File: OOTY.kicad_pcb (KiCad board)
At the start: 2 copper layers, 0 parts

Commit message: phase 3: PCB setup (85x55 mm, 4 layers, rules, connectors placed), DRC 0 errors
Co-Authored-By: Claude Opus 5.5 <noreply@anthropic.com>
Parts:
- added C1: 100nF/50V, Capacitor_SMD:C_0402_1005Metric, F.Cu at (196.4, 101.0)
- added C10: 10uF/25V, Capacitor_SMD:C_0805_2012Metric, F.Cu at (227.4, 101.5)
- added C11: 100nF/50V, Capacitor_SMD:C_0402_1005Metric, F.Cu at (231.0, 101.0)
- added C12: 100nF/50V, Capacitor_SMD:C_0402_1005Metric, F.Cu at (233.9, 101.0)
- added C13: 10uF/25V, Capacitor_SMD:C_0805_2012Metric, F.Cu at (237.5, 101.5)
- added C14: 100nF/50V, Capacitor_SMD:C_0402_1005Metric, F.Cu at (241.2, 101.0)
- added C15: 100nF/50V, Capacitor_SMD:C_0402_1005Metric, F.Cu at (244.1, 101.0)
- added C16: 10uF/10V, Capacitor_SMD:C_0603_1608Metric, F.Cu at (247.5, 101.3)
- added C17: 100nF/50V, Capacitor_SMD:C_0402_1005Metric, F.Cu at (251.0, 101.0)
- added C18: 100nF/50V, Capacitor_SMD:C_0402_1005Metric, F.Cu at (253.8, 101.0)
- added C19: 10uF/10V, Capacitor_SMD:C_0603_1608Metric, F.Cu at (257.3, 101.3)
- added C2: 100nF/50V, Capacitor_SMD:C_0402_1005Metric, F.Cu at (199.3, 101.0)
- added C20: 100nF/50V, Capacitor_SMD:C_0402_1005Metric, F.Cu at (253.9, 104.0)
- added C21: 100nF/50V, Capacitor_SMD:C_0402_1005Metric, F.Cu at (256.8, 104.0)
- added C22: 100nF/50V, Capacitor_SMD:C_0402_1005Metric, F.Cu at (259.7, 104.0)
- added C23: 100nF/50V, Capacitor_SMD:C_0402_1005Metric, F.Cu at (262.5, 104.0)
- added C24: 4.7uF/16V, Capacitor_SMD:C_0603_1608Metric, F.Cu at (266.0, 104.3)
- added C25: 100nF/50V, Capacitor_SMD:C_0402_1005Metric, F.Cu at (269.4, 104.0)
- added C26: 10nF/50V, Capacitor_SMD:C_0402_1005Metric, F.Cu at (272.3, 104.0)
- added C27: 1uF/25V, Capacitor_SMD:C_0402_1005Metric, F.Cu at (196.4, 107.5)
- added C28: 100nF/50V, Capacitor_SMD:C_0402_1005Metric, F.Cu at (199.3, 107.5)
- added C29: 1uF/25V, Capacitor_SMD:C_0402_1005Metric, F.Cu at (202.2, 107.5)
- added C3: 10uF/10V, Capacitor_SMD:C_0603_1608Metric, F.Cu at (202.7, 101.3)
- added C30: 100nF/50V, Capacitor_SMD:C_0402_1005Metric, F.Cu at (205.0, 107.5)
- added C31: 100nF/50V, Capacitor_SMD:C_0402_1005Metric, F.Cu at (217.3, 107.5)
- added C32: 100nF/50V, Capacitor_SMD:C_0402_1005Metric, F.Cu at (220.2, 107.5)
- added C33: 10nF/50V, Capacitor_SMD:C_0402_1005Metric, F.Cu at (223.0, 107.5)
- added C34: 10nF/50V, Capacitor_SMD:C_0402_1005Metric, F.Cu at (225.9, 107.5)
- added C35: 10nF/50V, Capacitor_SMD:C_0402_1005Metric, F.Cu at (228.8, 107.5)
- added C36: 100nF/50V, Capacitor_SMD:C_0402_1005Metric, F.Cu at (231.6, 107.5)
- added C37: 1uF/25V, Capacitor_SMD:C_0402_1005Metric, F.Cu at (201.6, 111.1)
- added C38: 1uF/25V, Capacitor_SMD:C_0402_1005Metric, F.Cu at (204.5, 111.1)
- added C39: 1uF/25V, Capacitor_SMD:C_0402_1005Metric, F.Cu at (207.3, 111.1)
- added C4: 100nF/50V, Capacitor_SMD:C_0402_1005Metric, F.Cu at (206.2, 101.0)
- added C40: 1uF/25V, Capacitor_SMD:C_0402_1005Metric, F.Cu at (210.2, 111.1)
- added C41: 1uF/25V, Capacitor_SMD:C_0402_1005Metric, F.Cu at (213.1, 111.1)
- added C42: 1nF/50V, Capacitor_SMD:C_0402_1005Metric, F.Cu at (215.9, 111.1)
- added C43: 100nF/50V, Capacitor_SMD:C_0402_1005Metric, F.Cu at (252.8, 111.1)
- added C44: 100nF/50V, Capacitor_SMD:C_0402_1005Metric, F.Cu at (255.7, 111.1)
- added C45: 100nF/50V, Capacitor_SMD:C_0402_1005Metric, F.Cu at (258.5, 111.1)
- added C46: 100nF/50V, Capacitor_SMD:C_0402_1005Metric, F.Cu at (261.4, 111.1)
- added C47: 100nF/50V, Capacitor_SMD:C_0402_1005Metric, F.Cu at (264.3, 111.1)
- added C48: 100nF/50V, Capacitor_SMD:C_0402_1005Metric, F.Cu at (267.1, 111.1)
- added C49: 100nF/50V, Capacitor_SMD:C_0402_1005Metric, F.Cu at (270.0, 111.1)
- added C5: 6.8pF DNP, Capacitor_SMD:C_0402_1005Metric, F.Cu at (209.1, 101.0)
- added C50: 100nF/50V, Capacitor_SMD:C_0402_1005Metric, F.Cu at (272.9, 111.1)
- added C51: 100nF/50V, Capacitor_SMD:C_0402_1005Metric, F.Cu at (196.4, 115.7)
- added C52: 100nF/50V, Capacitor_SMD:C_0402_1005Metric, F.Cu at (199.3, 115.7)
- added C53: 100nF/50V, Capacitor_SMD:C_0402_1005Metric, F.Cu at (202.2, 115.7)
- added C54: 100nF/50V, Capacitor_SMD:C_0402_1005Metric, F.Cu at (205.0, 115.7)
- added C6: 22uF/25V, Capacitor_SMD:C_0805_2012Metric, F.Cu at (212.7, 101.5)
- added C7: 22uF/25V, Capacitor_SMD:C_0805_2012Metric, F.Cu at (217.2, 101.5)
- added C8: 100nF/50V, Capacitor_SMD:C_0402_1005Metric, F.Cu at (220.8, 101.0)
- added C9: 100nF/50V, Capacitor_SMD:C_0402_1005Metric, F.Cu at (223.7, 101.0)
- added D1: SMAJ5.0A, Diode_SMD:D_SMA, F.Cu at (109.5, 118.0)
- added D2: PWR, LED_SMD:LED_0603_1608Metric, F.Cu at (164.0, 103.5)
- added D3: HB, LED_SMD:LED_0603_1608Metric, F.Cu at (168.0, 103.5)
- added F1: PTC 2.6A, Fuse:Fuse_1812_4532Metric, F.Cu at (112.5, 136.5)
- added H1: M3, MountingHole:MountingHole_3.2mm_M3, F.Cu at (103.5, 103.5)
- added H2: M3, MountingHole:MountingHole_3.2mm_M3, F.Cu at (181.5, 103.5)
- added H3: M3, MountingHole:MountingHole_3.2mm_M3, F.Cu at (103.5, 151.5)
- added H4: M3, MountingHole:MountingHole_3.2mm_M3, F.Cu at (181.5, 151.5)
- added J1: TYPE-C-31-M-12, Connector_USB:USB_C_Receptacle_HRO_TYPE-C-31-M-12, F.Cu at (104.2, 127.5)
- added J2: SWD_HIL, Connector_PinHeader_1.27mm:PinHeader_2x05_P1.27mm_Vertical_SMD, F.Cu at (112.0, 110.5)
- added J3: OLED 0.91in, Connector_PinSocket_2.54mm:PinSocket_1x04_P2.54mm_Vertical, F.Cu at (122.0, 103.5)
- added J4: J_PWR, Connector_PinHeader_2.54mm:PinHeader_1x07_P2.54mm_Vertical, F.Cu at (112.0, 152.0)
- added J5: J_DBG, Connector_PinHeader_2.54mm:PinHeader_1x07_P2.54mm_Vertical, F.Cu at (131.1, 152.0)
- added J6: J_BUS, Connector_PinHeader_2.54mm:PinHeader_1x07_P2.54mm_Vertical, F.Cu at (182.0, 109.4)
- added J7: J_UART_ANA, Connector_PinHeader_2.54mm:PinHeader_1x07_P2.54mm_Vertical, F.Cu at (182.0, 128.4)
- added J8: J_IO, Connector_PinHeader_2.54mm:PinHeader_1x10_P2.54mm_Vertical, F.Cu at (150.1, 152.0)
- added L1: 2.2uH, Inductor_SMD:L_Changjiang_FXL0420, F.Cu at (123.5, 139.0)
- added Q1: 2N7002, Package_TO_SOT_SMD:SOT-23, F.Cu at (219.8, 112.3)
- added Q2: 2N7002, Package_TO_SOT_SMD:SOT-23, F.Cu at (208.9, 117.0)
- added R1: 5.1k, Resistor_SMD:R_0402_1005Metric, F.Cu at (260.7, 101.0)
- added R10: 10k, Resistor_SMD:R_0402_1005Metric, F.Cu at (208.1, 104.0)
- added R11: 39k, Resistor_SMD:R_0402_1005Metric, F.Cu at (211.0, 104.0)
- added R12: 10k, Resistor_SMD:R_0402_1005Metric, F.Cu at (213.9, 104.0)
- added R13: 100k, Resistor_SMD:R_0402_1005Metric, F.Cu at (216.8, 104.0)
- added R14: 68k, Resistor_SMD:R_0402_1005Metric, F.Cu at (219.7, 104.0)
- added R15: 10k, Resistor_SMD:R_0402_1005Metric, F.Cu at (222.6, 104.0)
- added R16: 10k, Resistor_SMD:R_0402_1005Metric, F.Cu at (207.9, 107.6)
- added R17: 1k, Resistor_SMD:R_0402_1005Metric, F.Cu at (210.8, 107.6)
- added R18: 50mR 1% 1W, Resistor_SMD:R_1206_3216Metric, F.Cu at (235.9, 108.2)
- added R19: 100mR 1% 1W, Resistor_SMD:R_1206_3216Metric, F.Cu at (241.5, 108.2)
- added R2: 5.1k, Resistor_SMD:R_0402_1005Metric, F.Cu at (263.6, 101.0)
- added R20: 2.2k, Resistor_SMD:R_0402_1005Metric, F.Cu at (245.7, 107.6)
- added R21: 2.2k, Resistor_SMD:R_0402_1005Metric, F.Cu at (248.7, 107.6)
- added R22: 10k, Resistor_SMD:R_0402_1005Metric, F.Cu at (251.6, 107.6)
- added R23: 100k, Resistor_SMD:R_0402_1005Metric, F.Cu at (254.5, 107.6)
- added R24: 100k, Resistor_SMD:R_0402_1005Metric, F.Cu at (257.4, 107.6)
- added R25: 100k, Resistor_SMD:R_0402_1005Metric, F.Cu at (260.3, 107.6)
- added R26: 100k, Resistor_SMD:R_0402_1005Metric, F.Cu at (263.2, 107.6)
- added R27: 100k, Resistor_SMD:R_0402_1005Metric, F.Cu at (266.1, 107.6)
- added R28: 100k, Resistor_SMD:R_0402_1005Metric, F.Cu at (269.0, 107.6)
- added R29: 100R, Resistor_SMD:R_0402_1005Metric, F.Cu at (271.9, 107.6)
- added R3: 100k, Resistor_SMD:R_0402_1005Metric, F.Cu at (266.5, 101.0)
- added R30: 10k, Resistor_SMD:R_0402_1005Metric, F.Cu at (223.7, 111.1)
- added R31: 22k, Resistor_SMD:R_0402_1005Metric, F.Cu at (226.6, 111.1)
- added R32: 100k, Resistor_SMD:R_0402_1005Metric, F.Cu at (229.6, 111.1)
- added R33: 30k, Resistor_SMD:R_0402_1005Metric, F.Cu at (232.5, 111.1)
- added R34: 24k, Resistor_SMD:R_0402_1005Metric, F.Cu at (235.4, 111.1)
- added R35: 16k, Resistor_SMD:R_0402_1005Metric, F.Cu at (238.3, 111.1)
- added R36: 100k, Resistor_SMD:R_0402_1005Metric, F.Cu at (241.2, 111.1)
- added R37: 10k, Resistor_SMD:R_0402_1005Metric, F.Cu at (212.8, 115.7)
- added R38: 100k, Resistor_SMD:R_0402_1005Metric, F.Cu at (215.8, 115.7)
- added R39: 100k, Resistor_SMD:R_0402_1005Metric, F.Cu at (218.7, 115.7)
- added R4: 22k, Resistor_SMD:R_0402_1005Metric, F.Cu at (269.5, 101.0)
- added R40: 4.7k, Resistor_SMD:R_0402_1005Metric, F.Cu at (221.6, 115.7)
- added R41: 4.7k, Resistor_SMD:R_0402_1005Metric, F.Cu at (224.5, 115.7)
- added R42: 4.7k, Resistor_SMD:R_0402_1005Metric, F.Cu at (227.4, 115.7)
- added R43: 4.7k, Resistor_SMD:R_0402_1005Metric, F.Cu at (230.3, 115.7)
- added R44: 10k, Resistor_SMD:R_0402_1005Metric, F.Cu at (233.2, 115.7)
- added R45: 100k, Resistor_SMD:R_0402_1005Metric, F.Cu at (236.1, 115.7)
- added R46: 100k, Resistor_SMD:R_0402_1005Metric, F.Cu at (239.0, 115.7)
- added R47: 1M, Resistor_SMD:R_0402_1005Metric, F.Cu at (241.9, 115.7)
- added R48: 1M, Resistor_SMD:R_0402_1005Metric, F.Cu at (244.9, 115.7)
- added R49: 1M, Resistor_SMD:R_0402_1005Metric, F.Cu at (247.8, 115.7)
- added R5: 1k, Resistor_SMD:R_0402_1005Metric, F.Cu at (272.4, 101.0)
- added R50: 1M, Resistor_SMD:R_0402_1005Metric, F.Cu at (250.7, 115.7)
- added R51: 1M, Resistor_SMD:R_0402_1005Metric, F.Cu at (253.6, 115.7)
- added R52: 1M, Resistor_SMD:R_0402_1005Metric, F.Cu at (256.5, 115.7)
- added R53: 1M, Resistor_SMD:R_0402_1005Metric, F.Cu at (259.4, 115.7)
- added R54: 1M, Resistor_SMD:R_0402_1005Metric, F.Cu at (262.3, 115.7)
- added R55: 1M, Resistor_SMD:R_0402_1005Metric, F.Cu at (265.2, 115.7)
- added R56: 1M, Resistor_SMD:R_0402_1005Metric, F.Cu at (268.1, 115.7)
- added R57: 100R, Resistor_SMD:R_0402_1005Metric, F.Cu at (214.2, 120.4)
- added R58: 100R, Resistor_SMD:R_0402_1005Metric, F.Cu at (217.1, 120.4)
- added R59: 100R, Resistor_SMD:R_0402_1005Metric, F.Cu at (220.0, 120.4)
- added R6: 22k, Resistor_SMD:R_0402_1005Metric, F.Cu at (196.5, 104.0)
- added R60: 100R, Resistor_SMD:R_0402_1005Metric, F.Cu at (222.9, 120.4)
- added R61: 100R, Resistor_SMD:R_0402_1005Metric, F.Cu at (225.8, 120.4)
- added R62: 100R, Resistor_SMD:R_0402_1005Metric, F.Cu at (228.7, 120.4)
- added R63: 100R, Resistor_SMD:R_0402_1005Metric, F.Cu at (231.6, 120.4)
- added R64: 100R, Resistor_SMD:R_0402_1005Metric, F.Cu at (234.5, 120.4)
- added R65: 100R, Resistor_SMD:R_0402_1005Metric, F.Cu at (237.4, 120.4)
- added R66: 100R, Resistor_SMD:R_0402_1005Metric, F.Cu at (240.4, 120.4)
- added R67: 100R, Resistor_SMD:R_0402_1005Metric, F.Cu at (243.3, 120.4)
- added R68: 100R, Resistor_SMD:R_0402_1005Metric, F.Cu at (246.2, 120.4)
- added R69: 100R, Resistor_SMD:R_0402_1005Metric, F.Cu at (249.1, 120.4)
- added R7: 10k, Resistor_SMD:R_0402_1005Metric, F.Cu at (199.4, 104.0)
- added R70: 100R, Resistor_SMD:R_0402_1005Metric, F.Cu at (252.0, 120.4)
- added R71: 100R, Resistor_SMD:R_0402_1005Metric, F.Cu at (254.9, 120.4)
- added R72: 100R, Resistor_SMD:R_0402_1005Metric, F.Cu at (257.8, 120.4)
- added R73: 100R, Resistor_SMD:R_0402_1005Metric, F.Cu at (260.7, 120.4)
- added R74: 100R, Resistor_SMD:R_0402_1005Metric, F.Cu at (263.6, 120.4)
- added R75: 100R, Resistor_SMD:R_0402_1005Metric, F.Cu at (266.5, 120.4)
- added R8: 100k, Resistor_SMD:R_0402_1005Metric, F.Cu at (202.3, 104.0)
- added R9: 39k, Resistor_SMD:R_0402_1005Metric, F.Cu at (205.2, 104.0)
- added TP1: VBUS, TestPoint:TestPoint_Pad_D1.5mm, F.Cu at (225.9, 104.8)
- added TP10: VIO, TestPoint:TestPoint_Pad_D1.5mm, F.Cu at (244.4, 111.9)
- added TP2: +5V, TestPoint:TestPoint_Pad_D1.5mm, F.Cu at (229.4, 104.8)
- added TP3: +3V3, TestPoint:TestPoint_Pad_D1.5mm, F.Cu at (233.0, 104.8)
- added TP4: 5V_SW, TestPoint:TestPoint_Pad_D1.5mm, F.Cu at (236.5, 104.8)
- added TP5: 5V_DUT, TestPoint:TestPoint_Pad_D1.5mm, F.Cu at (240.1, 104.8)
- added TP6: 3V3_SW, TestPoint:TestPoint_Pad_D1.5mm, F.Cu at (243.6, 104.8)
- added TP7: 3V3_DUT, TestPoint:TestPoint_Pad_D1.5mm, F.Cu at (247.2, 104.8)
- added TP8: GND, TestPoint:TestPoint_Pad_D1.5mm, F.Cu at (250.7, 104.8)
- added TP9: BOOT0, TestPoint:TestPoint_Pad_D1.5mm, F.Cu at (214.1, 108.3)
- added U1: TPD4E05U06DQAR, Package_SON:USON-10_2.5x1.0mm_P0.5mm, F.Cu at (112.5, 131.0)
- added U10: INA226AIDGSR, Package_SO:MSOP-10_3x3mm_P0.5mm, F.Cu at (127.5, 134.0)
- added U11: TLV9001IDBVR, Package_TO_SOT_SMD:SOT-23-5, F.Cu at (197.6, 112.4)
- added U12: TPS2116DRLR, Package_TO_SOT_SMD:SOT-583-8, F.Cu at (149.0, 130.0)
- added U13: AP2127K-ADJTRG1, Package_TO_SOT_SMD:SOT-23-5, F.Cu at (248.8, 112.4)
- added U14: SN74LVC8T245PWR, Package_SO:TSSOP-24_4.4x7.8mm_P0.65mm, F.Cu at (158.0, 139.0)
- added U15: SN74LVC8T245PWR, Package_SO:TSSOP-24_4.4x7.8mm_P0.65mm, F.Cu at (168.0, 139.0)
- added U16: SN74LVC1T45DBVR, Package_TO_SOT_SMD:SOT-23-6, F.Cu at (272.2, 117.0)
- added U17: SN74LVC1T45DBVR, Package_TO_SOT_SMD:SOT-23-6, F.Cu at (197.6, 121.7)
- added U18: TCA9517ADGKR, Package_SO:VSSOP-8_3x3mm_P0.65mm, F.Cu at (203.9, 121.7)
- added U19: SN74LVC1T45DBVR, Package_TO_SOT_SMD:SOT-23-6, F.Cu at (210.1, 121.7)
- added U2: USBLC6-2SC6, Package_TO_SOT_SMD:SOT-23-6, F.Cu at (112.5, 124.0)
- added U20: TPD4E05U06DQAR, Package_SON:USON-10_2.5x1.0mm_P0.5mm, F.Cu at (269.4, 121.5)
- added U21: TPD4E05U06DQAR, Package_SON:USON-10_2.5x1.0mm_P0.5mm, F.Cu at (272.3, 121.5)
- added U22: TPD4E05U06DQAR, Package_SON:USON-10_2.5x1.0mm_P0.5mm, F.Cu at (196.4, 126.2)
- added U23: TPD4E05U06DQAR, Package_SON:USON-10_2.5x1.0mm_P0.5mm, F.Cu at (199.3, 126.2)
- added U24: TPD4E05U06DQAR, Package_SON:USON-10_2.5x1.0mm_P0.5mm, F.Cu at (202.2, 126.2)
- added U25: TPD4E05U06DQAR, Package_SON:USON-10_2.5x1.0mm_P0.5mm, F.Cu at (205.1, 126.2)
- added U26: TPD4E05U06DQAR, Package_SON:USON-10_2.5x1.0mm_P0.5mm, F.Cu at (208.0, 126.2)
- added U27: TPD4E05U06DQAR, Package_SON:USON-10_2.5x1.0mm_P0.5mm, F.Cu at (210.9, 126.2)
- added U3: TLV62569DBVR, Package_TO_SOT_SMD:SOT-23-5, F.Cu at (117.5, 139.0)
- added U4: AP22653W6-7, Package_TO_SOT_SMD:SOT-23-6, F.Cu at (109.0, 144.5)
- added U5: AP22653W6-7, Package_TO_SOT_SMD:SOT-23-6, F.Cu at (115.0, 144.5)
- added U6: AP22653W6-7, Package_TO_SOT_SMD:SOT-23-6, F.Cu at (121.0, 144.5)
- added U7: AP22653W6-7, Package_TO_SOT_SMD:SOT-23-6, F.Cu at (127.0, 144.5)
- added U8: STM32G431RBT6, Package_QFP:LQFP-64_10x10mm_P0.5mm, F.Cu at (134.0, 123.0)
- added U9: INA226AIDGSR, Package_SO:MSOP-10_3x3mm_P0.5mm, F.Cu at (106.0, 139.5)
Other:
- board outline added: 85 x 55 mm
- copper layers 2 -> 4

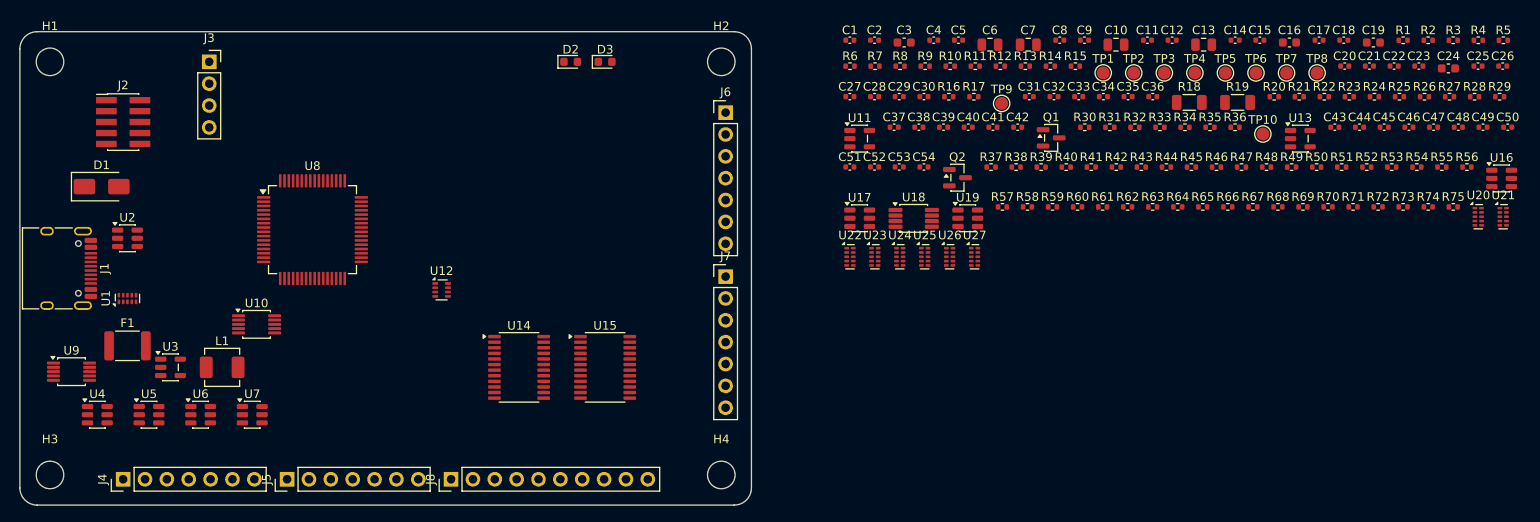
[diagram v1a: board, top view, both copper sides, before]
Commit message: phase 4: placement complete, DRC 0 errors, renders exported (awaiting checkpoint)
Co-Authored-By: Claude Opus 5.5 <noreply@anthropic.com>
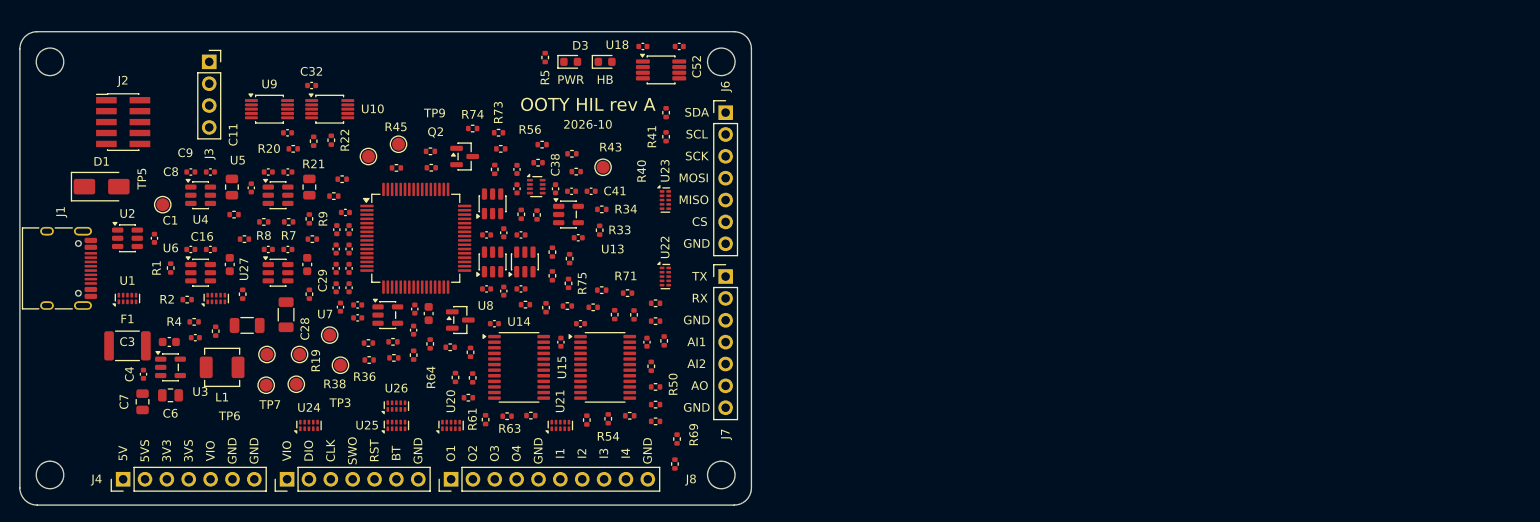
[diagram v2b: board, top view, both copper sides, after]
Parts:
- moved R4 152.7 mm to (120.3, 133.7)
- moved R3 147.7 mm to (122.8, 134.8), turned to 90 degrees
- moved R2 147.3 mm to (119.4, 131.1)
- moved R1 145.6 mm to (117.5, 127.5), turned to 90 degrees
- moved C26 137.6 mm to (136.8, 127.5), turned to 90 degrees
- moved C25 135.1 mm to (137.2, 132.0), turned to 90 degrees
- moved R29 134.5 mm to (140.5, 136.2)
- moved R28 126.9 mm to (145.8, 137.6), turned to 90 degrees
- moved C19 126.5 mm to (133.4, 127.0), turned to 90 degrees
- moved C16 125.8 mm to (124.4, 127.0), turned to 90 degrees
- moved C23 125.7 mm to (138.2, 123.0), turned to 90 degrees
- moved C18 125.1 mm to (131.1, 125.3)
- moved C17 124.5 mm to (128.9, 125.3)
- moved TP5 124.4 mm to (116.6, 120.1)
- moved C15 124.3 mm to (122.1, 125.3)
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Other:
- board text added: "2026-10"
- board text added: "3V3"
- board text added: "3VS"
- board text added: "5V"
- board text added: "5VS"
- board text added: "AI1"
- board text added: "AI2"
- board text added: "AO"
- board text added: "BT"
- board text added: "CLK"
- board text added: "CS"
- board text added: "DIO"
- board text added: "GND"
- board text added: "HB"
- board text added: "I1"
- board text added: "I2"
- board text added: "I3"
- board text added: "I4"
- board text added: "MISO"
- board text added: "MOSI"
- board text added: "O1"
- board text added: "O2"
- board text added: "O3"
- board text added: "O4"
- board text added: "OOTY HIL rev A"
- board text added: "PWR"
- board text added: "RST"
- board text added: "RX"
- board text added: "SCK"
- board text added: "SCL"
- board text added: "SDA"
- board text added: "SWO"
- board text added: "TX"
- board text added: "VIO"

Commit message: fix: redo PCB placement and rules after the placement review
Rules: annular ring 0.15 mm, smallest via 0.5/0.2 mm, silkscreen text 1.0/0.15 mm,
VIO net class limited to power nets, VBUS/+5V 1.5 mm, 7 mm copper keepout around M3 holes,
USB-C flush with the board edge.

Placement: MCU rotated 180 deg so USB, SWD probe and SPI/analog pins face their blocks;
TLV62569 cell per datasheet (Cin on VIN, inductor off SW, Cout at its output, FB divider
on the FB side); DUT rail switches, shunts and rail ESD above J_PWR; SWD/RESET/BOOT drivers
above J_DBG; translators above J_IO; ESD channels next to their header pins; VIO mux + LDO
under the OLED module; LEDs and buttons in the top-right corner.

Tooling: decoupling capacitors target the exact pin they decouple and are checked against
it (50/50 within limits); silkscreen of key parts reserved before auto-placement, no
reference over another part; header references between label rows; test points labelled
with their net; ratsnest plot for placement review.

DRC with schematic parity: 0 errors, 0 parity issues.

Co-Authored-By: Claude Opus 5.5 <noreply@anthropic.com>
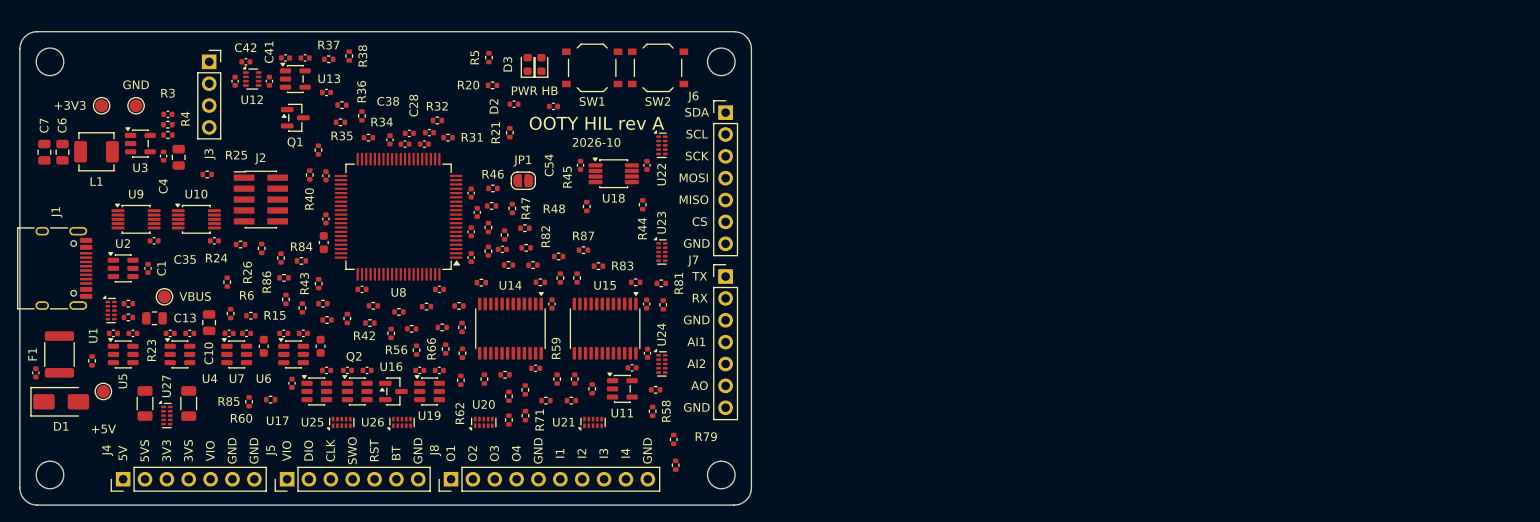
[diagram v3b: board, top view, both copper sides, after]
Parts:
- removed TP10: VIO, TestPoint:TestPoint_Pad_D1.5mm
- removed TP5: 5V_DUT, TestPoint:TestPoint_Pad_D1.5mm
- removed TP6: 3V3_SW, TestPoint:TestPoint_Pad_D1.5mm
- removed TP7: 3V3_DUT, TestPoint:TestPoint_Pad_D1.5mm
- removed TP8: GND, TestPoint:TestPoint_Pad_D1.5mm
- removed TP9: BOOT0, TestPoint:TestPoint_Pad_D1.5mm
- added C55: 100nF/50V, Capacitor_SMD:C_0402_1005Metric, F.Cu at (172.9, 115.5)
- added C56: 100nF/50V, Capacitor_SMD:C_0402_1005Metric, F.Cu at (146.5, 139.3)
- added C57: 100nF/50V, Capacitor_SMD:C_0402_1005Metric, F.Cu at (148.7, 139.3)
- added JP1: BOOT0, Jumper:SolderJumper-2_P1.3mm_Open_RoundedPad1.0x1.5mm, F.Cu at (158.5, 117.3)
- added R76: 100R, Resistor_SMD:R_0402_1005Metric, F.Cu at (158.8, 125.1)
- added R77: 100R, Resistor_SMD:R_0402_1005Metric, F.Cu at (174.7, 131.7)
- added R78: 100R, Resistor_SMD:R_0402_1005Metric, F.Cu at (176.0, 147.4)
- added R79: 100R, Resistor_SMD:R_0402_1005Metric, F.Cu at (176.2, 150.4)
- added R80: 100R, Resistor_SMD:R_0402_1005Metric, F.Cu at (171.6, 129.1)
- added R81: 100R, Resistor_SMD:R_0402_1005Metric, F.Cu at (174.5, 129.2)
- added R82: 100R, Resistor_SMD:R_0402_1005Metric, F.Cu at (164.7, 128.6)
- added R83: 100R, Resistor_SMD:R_0402_1005Metric, F.Cu at (167.2, 127.2)
- added R84: 100R, Resistor_SMD:R_0402_1005Metric, F.Cu at (132.7, 126.6)
- added R85: 100R, Resistor_SMD:R_0402_1005Metric, F.Cu at (126.6, 143.0)
- added R86: 100R, Resistor_SMD:R_0402_1005Metric, F.Cu at (130.3, 126.3)
- added R87: 100R, Resistor_SMD:R_0402_1005Metric, F.Cu at (165.5, 125.4)
- added SW1: BTN1, Button_Switch_SMD:SW_Push_1P1T_XKB_TS-1187A, F.Cu at (166.5, 104.2)
- added SW2: BTN2, Button_Switch_SMD:SW_Push_1P1T_XKB_TS-1187A, F.Cu at (174.2, 104.2)
- C24: value 4.7uF/16V -> 100nF/50V; footprint Capacitor_SMD:C_0603_1608Metric -> Capacitor_SMD:C_0402_1005Metric
- C25: value 100nF/50V -> 4.7uF/16V; footprint Capacitor_SMD:C_0402_1005Metric -> Capacitor_SMD:C_0603_1608Metric
- C26, C33, C34, C35: value 10nF/50V -> 100nF/50V
- C27, C37, C38: value 1uF/25V -> 10nF/50V
- C28, C30, C43, C44: value 100nF/50V -> 1uF/25V
- C29, C39: value 1uF/25V -> 100nF/50V
- C3: value 10uF/10V -> 10uF/25V; footprint Capacitor_SMD:C_0603_1608Metric -> Capacitor_SMD:C_0805_2012Metric
- C36: value 100nF/50V -> 10nF/50V
- C42: value 1nF/50V -> 1uF/25V
- C45: value 100nF/50V -> 1nF/50V
- R11: value 39k -> 100k
- R12: value 10k -> 39k
- R13, R26: value 100k -> 10k
- R14: value 68k -> 100k
- R15: value 10k -> 68k
- R17: value 1k -> 100k
- R18: value 50mR 1% 1W -> 10k; footprint Resistor_SMD:R_1206_3216Metric -> Resistor_SMD:R_0402_1005Metric
- R19: value 100mR 1% 1W -> 1k; footprint Resistor_SMD:R_1206_3216Metric -> Resistor_SMD:R_0402_1005Metric
- R20, R21: value 2.2k -> 10k
- R22: value 10k -> 50mR 1% 1W; footprint Resistor_SMD:R_0402_1005Metric -> Resistor_SMD:R_1206_3216Metric
- R23: value 100k -> 100mR 1% 1W; footprint Resistor_SMD:R_0402_1005Metric -> Resistor_SMD:R_1206_3216Metric
- R24, R25: value 100k -> 2.2k
- R29: value 100R -> 100k
- R30: value 10k -> 100k
- R31: value 22k -> 100k
- R33: value 30k -> 100R
- R34: value 24k -> 10k
- R35: value 16k -> 22k
- R37: value 10k -> 30k
- R38: value 100k -> 24k
- R39: value 100k -> 16k
- R40, R42, R43: value 4.7k -> 100k
- R41: value 4.7k -> 10k
- R44: value 10k -> 4.7k
- R45, R46: value 100k -> 4.7k
- R47: value 1M -> 4.7k
- R48: value 1M -> 10k
- R49, R50: value 1M -> 100k
- R57, R58, R59, R60, R61, R62, R63, R64, R65, R66, R67, R68: value 100R -> 1M
- TP4: value 5V_SW -> GND
- U8: value STM32G431RBT6 -> STM32G431MBT6; footprint Package_QFP:LQFP-64_10x10mm_P0.5mm -> Package_QFP:LQFP-80_12x12mm_P0.5mm
- moved C52 59.6 mm to (131.6, 140.8), turned to 90 degrees
- moved R25 52.5 mm to (121.8, 116.6), turned to 0 degrees
- moved C51 49.4 mm to (140.3, 139.3)
- moved C44 44.4 mm to (133.1, 103.0), turned to 0 degrees
- moved C42 43.7 mm to (126.3, 103.5)
- moved R40 41.6 mm to (133.7, 116.7)
- moved U24 41.6 mm to (174.6, 138.6), turned to 0 degrees
- moved C40 41.1 mm to (125.0, 105.8), turned to 90 degrees
- moved TP3 41.0 mm to (109.5, 108.6)
- moved C45 39.9 mm to (135.6, 107.1)
- moved R23 39.8 mm to (119.6, 143.2), turned to 90 degrees
- moved C41 39.5 mm to (129.0, 105.8), turned to 90 degrees
- moved C43 39.3 mm to (130.9, 103.0)
- moved C2 38.4 mm to (101.8, 139.6)
- moved R37 38.3 mm to (135.9, 103.2), turned to 0 degrees
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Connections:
- C30 pad 1: /mcu/NRST -> +3V3
- C31 pad 1: +3V3 -> /mcu/NRST
- C32 pad 1: +3V3 -> /mcu/BTN1
- C33 pad 1: AIN1_ADC -> /mcu/BTN2
- C34 pad 1: AIN2_ADC -> +3V3
- C35 pad 1: VIO_MON -> +3V3
- C36 pad 1: +3V3 -> AIN1_ADC
- C37 pad 1: +5V -> AIN2_ADC
- C38 pad 1: /vio/VIO_LDO -> VIO_MON
- C39 pad 1: VIO -> +3V3
- C40 pad 1: +5V -> 5V_DUT
- C42 pad 1: /vio/VIO_LDO -> VIO
- C42 pad 2: /vio/VIO_ADJ -> GND
- C43 pad 1: +3V3 -> +5V
- C44 pad 1: VIO -> /vio/VIO_LDO
- C45 pad 1: +3V3 -> /vio/VIO_LDO
- C45 pad 2: GND -> /vio/VIO_ADJ
- C46 pad 1: VIO -> +3V3
- C47 pad 1: +3V3 -> VIO
- C48 pad 1: VIO -> +3V3
- C49 pad 1: +3V3 -> VIO
- C50 pad 1: VIO -> +3V3
- C53 pad 1: +3V3 -> VIO
- D1 pad 1: VBUS -> +5V
- R11 pad 1: /power/ILIM_3V3SW -> EN_5V
- R11 pad 2: GND -> +5V
- R12 pad 1: FAULT_3V3SW -> /power/ILIM_3V3SW
- R12 pad 2: +3V3 -> GND
- R13 pad 1: EN_3V3SW -> FAULT_3V3SW
- R13 pad 2: GND -> +3V3
- R14 pad 1: /power/ILIM_3V3 -> EN_3V3SW
- R15 pad 1: FAULT_3V3 -> /power/ILIM_3V3
- R15 pad 2: +3V3 -> GND
- R16 pad 1: /mcu/BOOT0 -> FAULT_3V3
- R16 pad 2: GND -> +3V3
- R17 pad 1: /mcu/LED_HB -> EN_3V3
- R17 pad 2: /mcu/LED_HB_A -> +3V3
- R18 pad 1: 5V_SW_PRE -> /mcu/BOOT0
- R18 pad 2: 5V_SW -> GND
- R19 pad 1: 3V3_SW_PRE -> /mcu/LED_HB
- R19 pad 2: 3V3_SW -> /mcu/LED_HB_A
- R20 pad 1: I2C_INT_SDA -> /mcu/BTN1
- R21 pad 1: I2C_INT_SCL -> /mcu/BTN2
- R22 pad 1: INA_ALERT -> 5V_SW_PRE
- R22 pad 2: +3V3 -> 5V_SW
- R23 pad 1: AIN1 -> 3V3_SW_PRE
- R23 pad 2: AIN1_ADC -> 3V3_SW
- R24 pad 1: AIN1_ADC -> I2C_INT_SDA
- R24 pad 2: GND -> +3V3
- R25 pad 1: AIN2 -> I2C_INT_SCL
- R25 pad 2: AIN2_ADC -> +3V3
- R26 pad 1: AIN2_ADC -> INA_ALERT
- R26 pad 2: GND -> +3V3
- R27 pad 1: VIO -> AIN1
- R27 pad 2: VIO_MON -> AIN1_ADC
- R28 pad 1: VIO_MON -> AIN1_ADC
- R29 pad 1: /sensing/AOUT_BUF -> AIN2
- R29 pad 2: AOUT -> AIN2_ADC
- R30 pad 1: +5V -> AIN2_ADC
- R30 pad 2: VIO_PR1 -> GND
- R31 pad 1: VIO_PR1 -> VIO
- R31 pad 2: GND -> VIO_MON
- R32 pad 1: VIO_MODE -> VIO_MON
- R33 pad 1: /vio/VIO_LDO -> /sensing/AOUT_BUF
- R33 pad 2: /vio/VIO_ADJ -> AOUT
- R34 pad 1: /vio/VIO_ADJ -> +5V
- R34 pad 2: GND -> VIO_PR1
- R35 pad 1: /vio/VIO_ADJ -> VIO_PR1
- R35 pad 2: /vio/VSEL_D -> GND
- R36 pad 1: VIO_VSEL -> VIO_MODE
- R37 pad 1: LS_OE_N -> /vio/VIO_LDO
- R37 pad 2: +3V3 -> /vio/VIO_ADJ
- R38 pad 1: SWCLK_DIR -> /vio/VIO_ADJ
- R39 pad 1: SWDIO_DIR -> /vio/VIO_ADJ
- R39 pad 2: GND -> /vio/VSEL_D
- R40 pad 1: I2C_SCL -> VIO_VSEL
- R40 pad 2: VIO -> GND
- R41 pad 1: I2C_SDA -> LS_OE_N
- R41 pad 2: VIO -> +3V3
- R42 pad 1: I2C_DUT_SCL_MCU -> SWCLK_DIR
- R42 pad 2: +3V3 -> GND
- R43 pad 1: I2C_DUT_SDA_MCU -> SWDIO_DIR
- R43 pad 2: +3V3 -> GND
- R44 pad 1: I2C_DUT_EN -> I2C_SCL
- R44 pad 2: GND -> VIO
- R45 pad 1: RESET_DUT_CTL -> I2C_SDA
- R45 pad 2: GND -> VIO
- R46 pad 1: BOOT_DIR -> I2C_DUT_SCL_MCU
- R46 pad 2: GND -> +3V3
- R47 pad 1: IN1_B -> I2C_DUT_SDA_MCU
- R47 pad 2: GND -> +3V3
- R48 pad 1: IN2_B -> I2C_DUT_EN
- R49 pad 1: IN3_B -> RESET_DUT_CTL
- R50 pad 1: IN4_B -> BOOT_DIR
- R51 pad 1: SPI_MISO_B -> IN1_B
- R52 pad 1: SWCLK_B -> IN2_B
- R53 pad 1: BOOT_B -> IN3_B
- R54 pad 1: UART_RX_B -> IN4_B
- R54 pad 2: VIO -> GND
- R55 pad 1: SWO_DUT_B -> SPI_MISO_B
- R55 pad 2: VIO -> GND
- R56 pad 1: SWDIO_B -> SWCLK_B
- R56 pad 2: VIO -> GND
- R57 pad 1: OUT1_B -> BOOT_B
- R57 pad 2: /connectors/OUT1 -> GND
- R58 pad 1: OUT2_B -> UART_RX_B
- R58 pad 2: /connectors/OUT2 -> VIO
- R59 pad 1: OUT3_B -> SWO_DUT_B
- R59 pad 2: /connectors/OUT3 -> VIO
- R60 pad 1: OUT4_B -> SWDIO_B
- R60 pad 2: /connectors/OUT4 -> VIO
- R61 pad 1: UART_TX_B -> OUT1_B
- R61 pad 2: /connectors/TX -> GND
- R62 pad 1: SPI_SCK_B -> OUT2_B
- R62 pad 2: /connectors/SPI_SCK -> GND
- R63 pad 1: SPI_MOSI_B -> OUT3_B
- R63 pad 2: /connectors/SPI_MOSI -> GND
- R64 pad 1: SPI_CS_B -> OUT4_B
- R64 pad 2: /connectors/SPI_CS -> GND
- R65 pad 1: IN1_B -> SPI_SCK_B
- R65 pad 2: /connectors/IN1 -> GND
- R66 pad 1: IN2_B -> SPI_MOSI_B
- R66 pad 2: /connectors/IN2 -> GND
- R67 pad 1: IN3_B -> UART_TX_B
- R67 pad 2: /connectors/IN3 -> VIO
- R68 pad 1: IN4_B -> SPI_CS_B
- R68 pad 2: /connectors/IN4 -> VIO
- R69 pad 1: UART_RX_B -> OUT1_B
- R69 pad 2: /connectors/RX -> /connectors/OUT1
- R70 pad 1: SPI_MISO_B -> OUT2_B
- R70 pad 2: /connectors/SPI_MISO -> /connectors/OUT2
- R71 pad 1: SWO_DUT_B -> OUT3_B
- R71 pad 2: /connectors/SWO -> /connectors/OUT3
- R72 pad 1: SWCLK_B -> OUT4_B
- R72 pad 2: /connectors/SWCLK -> /connectors/OUT4
- R73 pad 1: SWDIO_B -> UART_TX_B
- R73 pad 2: /connectors/SWDIO -> /connectors/TX
- R74 pad 1: RESET_OD -> SPI_SCK_B
- R74 pad 2: /connectors/RESET -> /connectors/SPI_SCK
- R75 pad 1: BOOT_B -> SPI_MOSI_B
- R75 pad 2: /connectors/BOOT -> /connectors/SPI_MOSI
- TP4 pad 1: 5V_SW -> GND
- U12 pad 3: +5V -> 5V_DUT
- U15 pad 10: unconnected-(U15-A8-Pad10) -> GND
- U22 pad 1: /connectors/TX -> I2C_SDA
- U22 pad 2: /connectors/RX -> I2C_SCL
- U23 pad 4: I2C_SDA -> /connectors/TX
- U23 pad 5: I2C_SCL -> /connectors/RX
- U24 pad 1: /connectors/SWDIO -> AIN1
- U24 pad 2: /connectors/SWCLK -> AIN2
- U24 pad 4: /connectors/SWO -> AOUT
- U24 pad 5: /connectors/RESET -> unconnected-(U24-D2--Pad5)
- U25 pad 1: /connectors/BOOT -> /connectors/SWDIO
- U25 pad 2: AIN1 -> /connectors/SWCLK
- U25 pad 4: AIN2 -> /connectors/SWO
- U25 pad 5: AOUT -> /connectors/RESET
- U26 pad 1: VIO -> /connectors/BOOT
- U26 pad 2: unconnected-(U26-D1--Pad2) -> VIO
- U5 pad 3: +5V -> EN_5V
- U7 pad 3: +3V3 -> EN_3V3
- U8 pad 30: UART_TX_MCU -> unconnected-(U8-PE7-Pad30)
- U8 pad 31: GND -> unconnected-(U8-PE8-Pad31)
- U8 pad 32: +3V3 -> unconnected-(U8-PE9-Pad32)
- U8 pad 33: UART_RX_MCU -> /mcu/BTN2
- U8 pad 34: SWDIO_DIR -> /mcu/BTN1
- U8 pad 35: SWCLK_MCU -> /mcu/LED_HB
- U8 pad 36: VIO_VSEL -> unconnected-(U8-PE13-Pad36)
- U8 pad 37: SWDIO_MCU -> unconnected-(U8-PE14-Pad37)
- U8 pad 38: RESET_DUT_CTL -> unconnected-(U8-PE15-Pad38)
- U8 pad 39: BOOT_DUT_CTL -> UART_TX_MCU
- U8 pad 40: I2C_DUT_SCL_MCU -> GND
- U8 pad 41: I2C_DUT_SDA_MCU -> +3V3
- U8 pad 42: SPI_CS_MCU -> UART_RX_MCU
- U8 pad 43: LS_OE_N -> SWDIO_DIR
- U8 pad 44: /mcu/LED_HB -> SWCLK_MCU
- U8 pad 45: USB_DM -> VIO_VSEL
- U8 pad 46: USB_DP -> SWDIO_MCU
- U8 pad 47: GND -> EN_5V
- U8 pad 48: +3V3 -> EN_3V3
- U8 pad 49: /mcu/SWDIO_HIL -> BOOT_DIR
- U8 pad 50: /mcu/SWCLK_HIL -> GND
- U8 pad 51: I2C_INT_SCL -> +3V3
- U8 pad 52: IN1_MCU -> RESET_DUT_CTL
- U8 pad 53: IN2_MCU -> BOOT_DUT_CTL
- U8 pad 54: IN3_MCU -> I2C_DUT_SCL_MCU
- U8 pad 55: IN4_MCU -> I2C_DUT_SDA_MCU
- U8 pad 56: /mcu/SWO_HIL -> SPI_CS_MCU
- U8 pad 57: BOOT_DIR -> LS_OE_N
- U8 pad 58: FAULT_3V3 -> unconnected-(U8-PA10-Pad58)
- U8 pad 59: I2C_DUT_EN -> USB_DM
- U8 pad 60: I2C_INT_SDA -> USB_DP
- U8 pad 61: /mcu/BOOT0 -> GND
- U8 pad 62: INA_ALERT -> +3V3
- U8 pad 63: GND -> /mcu/SWDIO_HIL
- U8 pad 64: +3V3 -> /mcu/SWCLK_HIL
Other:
- board text added: "PWR HB"
- board text removed: "HB"
- board text removed: "PWR"
